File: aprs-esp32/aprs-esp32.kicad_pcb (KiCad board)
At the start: 4 copper layers, 100 x 100 mm, 47 parts, among them J1 GPS_CONNECTOR, J2 EXT_1WIRE, J3 PSU_CONN, J4 I2C, J5 M20-6102045, J6 RF_HI_LOW, J7 RF_OUT, J8 ESP PROGRAM, Q1 BSS138, Q2 BSS138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

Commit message: limpieza de esquematico
movi los level shifters a su propia pagina
movi la mayor parte de los conectores a una pagina separada
corregido: simbolos de pin desconectado faltantes
cambio: ESP renombrado a u2
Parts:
- renumbered ESP32-WROOM-32D1 to u2
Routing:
- added copper zone on B.Cu, net GND
- added copper zone on F.Cu, net GND
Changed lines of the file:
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@@
     (property "Sheetname" "")
     (attr smd)
-    (fp_text reference "ESP32-WROOM-32D1" (at -0.534725 12.101072 180) (layer "F.SilkS")
+    (fp_text reference "u2" (at -0.534725 12.101072 180) (layer "F.SilkS")
       (effects (font (size 1 1) (thickness 0.15)))
     )
@@
   (segment (start 63.785 97.1375) (end 63.2375 97.685) (width 0.2921) (layer "F.Cu") (net 54))
   (segment (start 63.785 94.215) (end 63.785 97.1375) (width 0.2921) (layer "F.Cu") (net 54))
-  (zone (net 18) (net_name "GND") (layer "In1.Cu") (name "GND") (hatch edge 0.508)
+  (zone (net 18) (net_name "GND") (layers "F.Cu" "In1.Cu" "B.Cu") (name "GND") (hatch edge 0.508)
     (priority 1)
     (connect_pads yes (clearance 0.8))

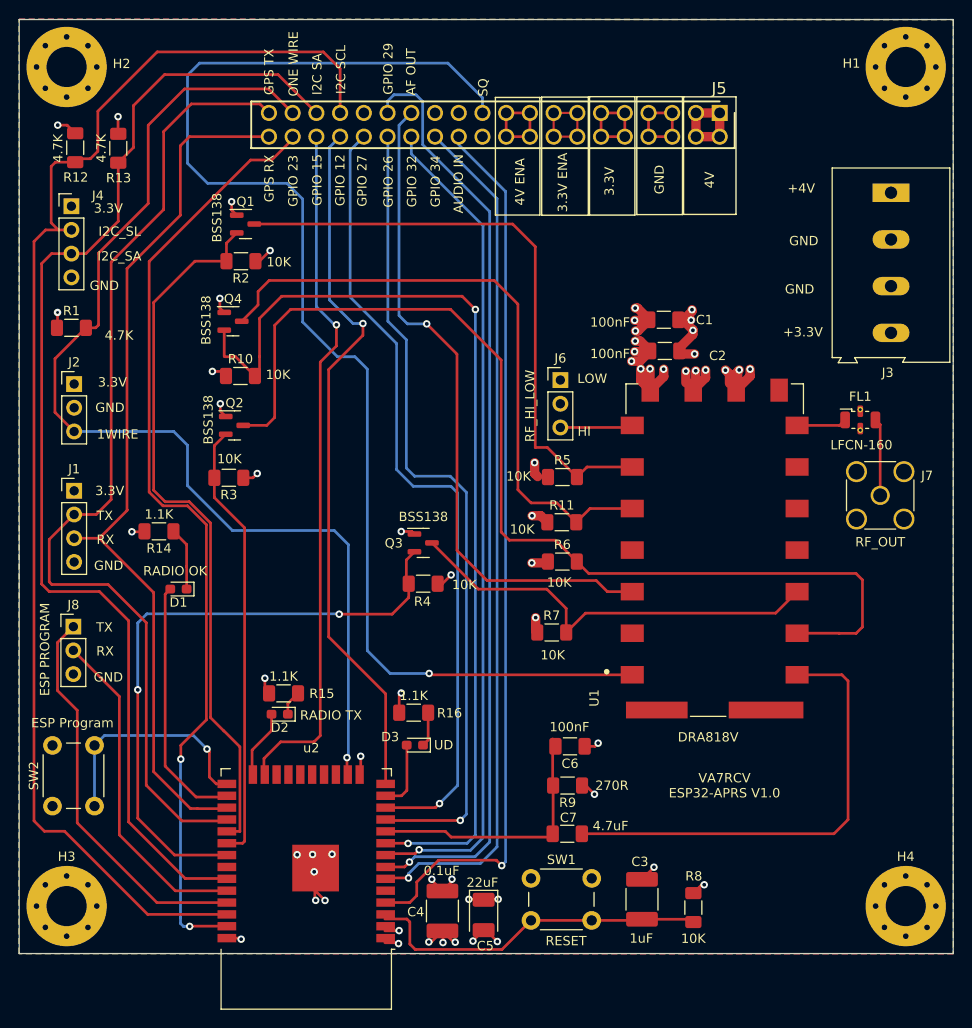
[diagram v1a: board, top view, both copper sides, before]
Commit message: multiple cambios en el ruteo
Todas las reglas de DRC pasan. solo hay warnings debido al silk screen
correcciones PCB:
- VDD para ESP y DRA ruteado via capacitores
- multiple conecciones a VDD cambiadas para evitar tombstoning

Optimizaciones PCB:
- algunos tracks fueron ruteados para reducir largo.
- todas las etiquetas fueron alienadas y/o movidas para hacer mas claro a quce componente corresponden.

cambios al proyecto:
- corregido tama;o de vias para +4v
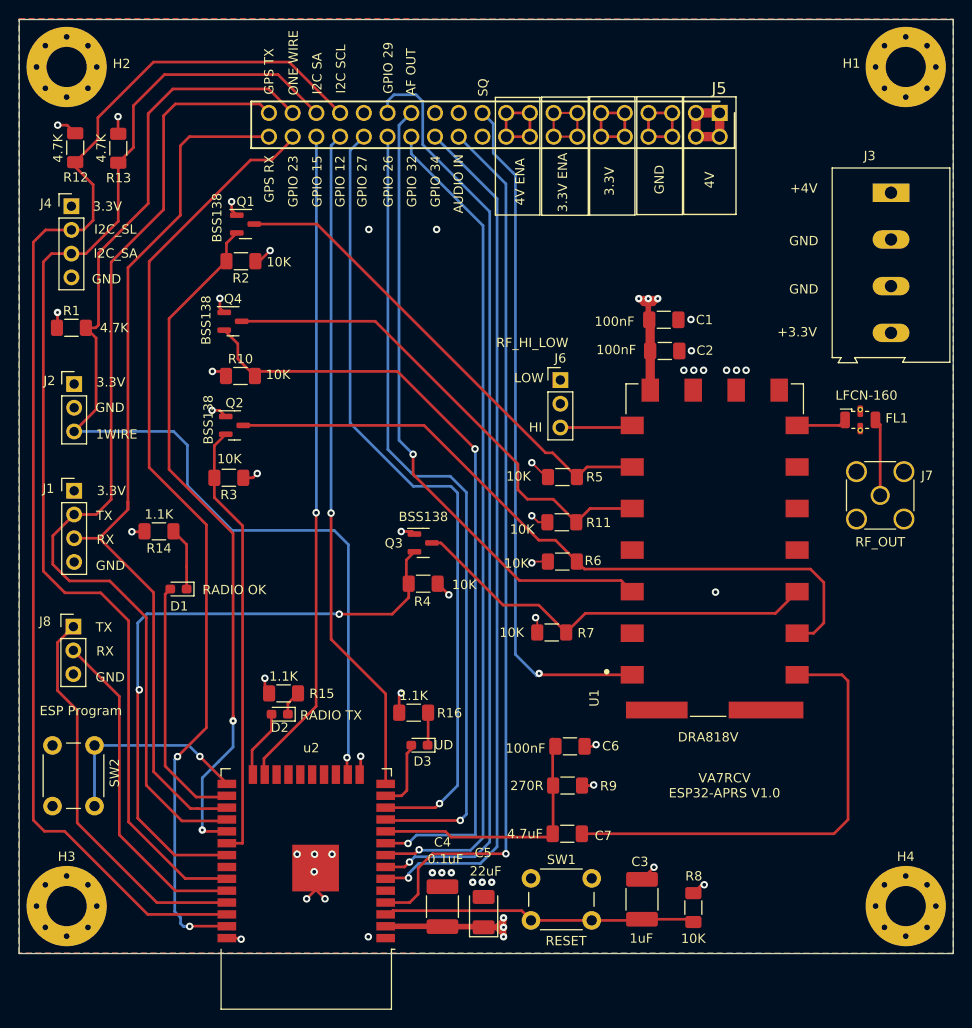
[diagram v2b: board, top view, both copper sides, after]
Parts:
- moved D3 0.49 mm to (62.9, 97.7)
- moved C4 0.46 mm to (65.3, 115.0), turned to 90 degrees
- moved C5 0.30 mm to (69.7, 115.6), turned to 90 degrees
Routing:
- net SQ: track 140.4 -> 73.1 mm
- net RADIO_TX_HIGH: track 112.3 -> 76.8 mm
- net GND: track 74.4 -> 39.4 mm, vias 30 -> 32
- net PTT_LOW: track 104.3 -> 84.8 mm
- net PTT_HIGH: track 67.4 -> 53.0 mm
- net RADIO_ENA_HIGH: track 64.7 -> 52.1 mm
- net +3V3: track 39.3 -> 48.4 mm, vias 17 -> 15
- net I2C_SCL: track 142.5 -> 137.7 mm
- net +4V: track 36.7 -> 32.1 mm, vias 13 -> 7
- net GPIO015: track 75.1 -> 71.1 mm
- net ESP_ENA: track 37.2 -> 33.4 mm
- net GPIO012: track 75.9 -> 72.1 mm
- net AF_OUT: track 71.8 -> 68.5 mm
- net ESP_PROG: track 24.9 -> 22.4 mm
- net RADIO_ENA_LOW: track 76.1 -> 74.4 mm, vias 0 -> 2
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
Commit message: pcb actualizado
- leds de status estan ahora juntos y visibles
- level shifters estan ahora juntos al centro
- capacitores de bypass estan ruteados correctamente.
- capacitores de bypass estan ordenados correctamente (valor ascendnte desde el circuito)
- lineas i2c estan ruteadas mas lejos del borde del pcb.
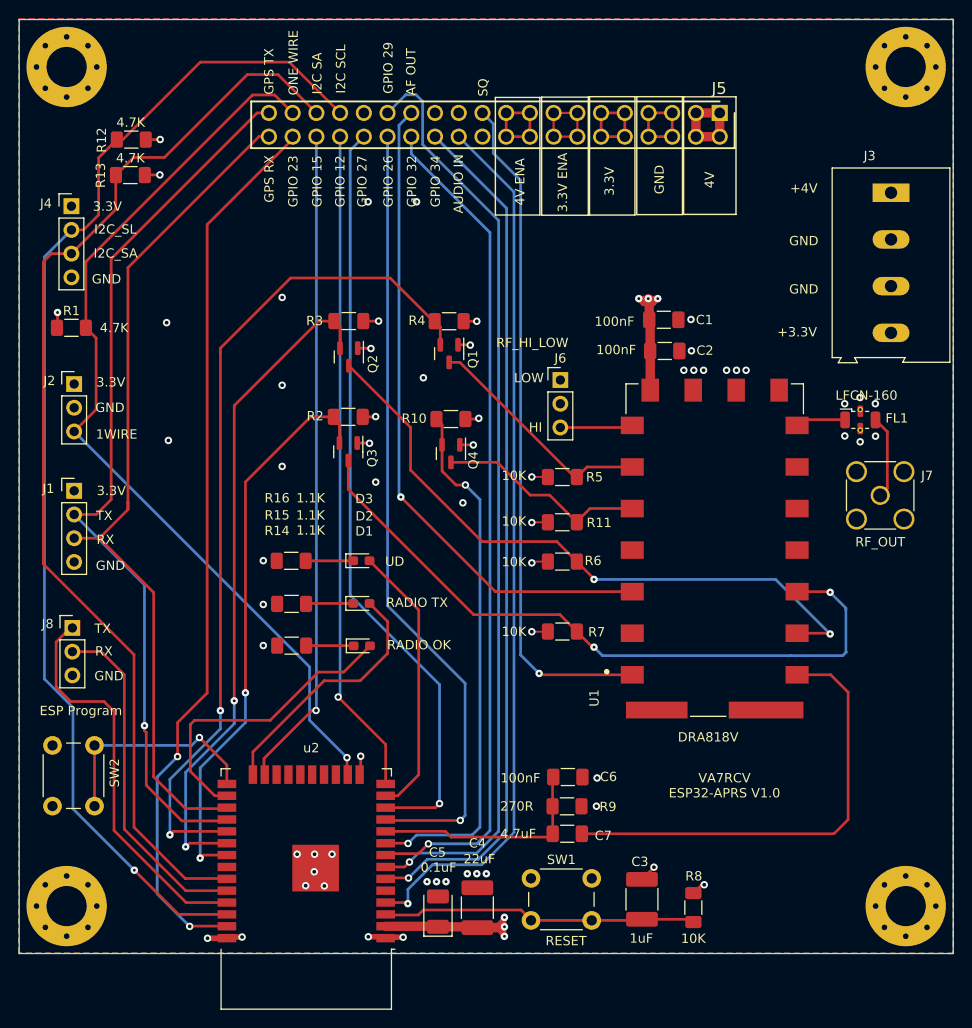
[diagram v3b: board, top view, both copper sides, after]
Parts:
- moved Q4 27.3 mm to (66.2, 66.5), turned to -90 degrees
- moved Q1 25.8 mm to (66.0, 55.8), turned to -90 degrees
- moved R4 23.2 mm to (66.0, 52.3)
- moved R10 23.0 mm to (66.2, 62.8), turned to 180 degrees
- moved R3 21.1 mm to (55.3, 52.3)
- moved R16 20.9 mm to (49.1, 78.0)
- moved D3 20.7 mm to (56.6, 77.9), turned to 0 degrees
- moved D1 20.6 mm to (56.7, 87.1), turned to 0 degrees
- moved R2 19.6 mm to (55.2, 62.5)
- moved R14 18.8 mm to (49.2, 87.0)
- moved D2 14.7 mm to (56.6, 82.5), turned to 0 degrees
- moved Q2 14.3 mm to (55.3, 56.1), turned to -90 degrees
- moved Q3 12.6 mm to (55.2, 66.3), turned to -90 degrees
- moved R15 9.62 mm to (49.2, 82.6)
- moved R12 6.07 mm to (32.0, 32.9), turned to 180 degrees
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- renumbered R4 to R2, R2 to R4
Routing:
- net PTT_HIGH: track 53.0 -> 22.7 mm
- net RADIO_RX_HIGH: track 44.9 -> 74.6 mm, vias 0 -> 2
- net PTT_LOW: track 84.8 -> 57.0 mm
- net RADIO_ENA_HIGH: track 52.1 -> 25.1 mm
- net RADIO_TX_LOW: track 46.9 -> 71.6 mm, vias 0 -> 2
- net GPIO014: track 7.55 -> 29.6 mm
- net GPIO02: track 7.82 -> 27.4 mm
- net ONE_WIRE: track 118.5 -> 99.3 mm
- net RADIO_ENA_LOW: track 74.4 -> 91.4 mm
- net GPS_TX: track 106.7 -> 95.7 mm, vias 0 -> 1
- net I2C_SCL: track 137.7 -> 127.6 mm, vias 0 -> 1
- net RADIO_TX_HIGH: track 76.8 -> 69.7 mm, vias 0 -> 2
- net RADIO_RX_LOW: track 67.1 -> 60.7 mm
- net I2C_SA: track 124.0 -> 117.5 mm
- net GPIO04: track 26.7 -> 32.7 mm
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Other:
- board text removed: "BSS138"

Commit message: cambios a la lineas de poder
-Modifique la isla de 4v para que sea mas peque;a
-Cambie el ruteo de varios tracks para hacerlos mas cortos
-modificado la ubicacion de algunas vias para que las lineas de tierra esten mas cercanas a los pads
-capacitores de bypass de ESP estan 1mm mas cerca.
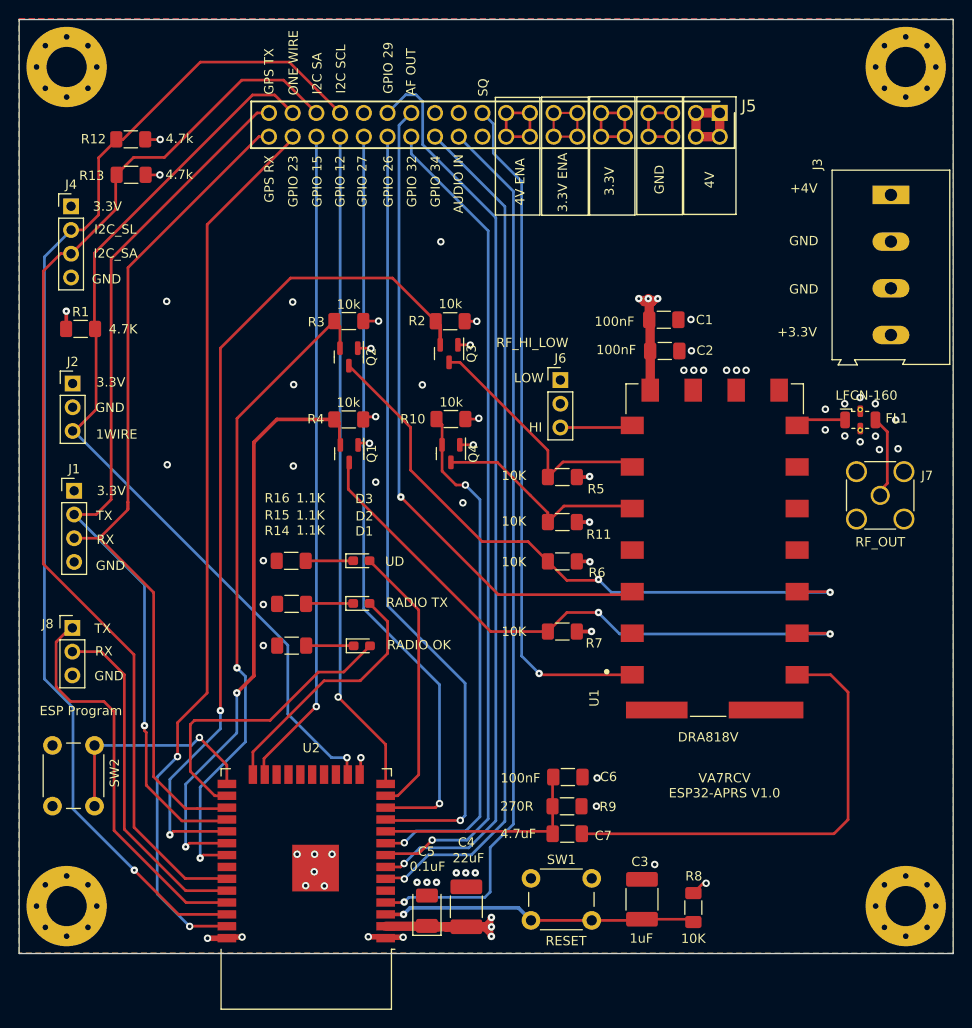
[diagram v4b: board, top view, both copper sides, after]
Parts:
- moved Q1 15.1 mm to (55.3, 66.5)
- moved Q3 15.1 mm to (66.0, 55.8)
- moved R4 15.0 mm to (55.3, 62.8)
- moved R2 15.0 mm to (66.1, 52.3)
- moved C4 1.18 mm to (67.9, 115.0)
- moved C5 1.18 mm to (63.7, 115.4)
- moved R1 0.99 mm to (26.6, 53.1)
- moved J3 0.23 mm to (113.3, 38.8)
- moved J2 0.17 mm to (25.7, 59.0)
- moved R13 0.09 mm to (32.0, 36.6)
- moved R12 0.07 mm to (31.9, 32.8)
- turned R11 to 180 degrees
- turned R6 to 180 degrees
- turned R5 to 180 degrees
- turned R7 to 180 degrees
- renumbered u2 to U2
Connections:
- Q1 pad 2: RADIO_ENA_LOW -> RADIO_TX_LOW
- Q1 pad 3: RADIO_ENA_HIGH -> RADIO_TX_HIGH
- Q2 pad 2: RADIO_TX_LOW -> RADIO_RX_LOW
- Q2 pad 3: RADIO_TX_HIGH -> RADIO_RX_HIGH
- Q3 pad 2: RADIO_RX_LOW -> RADIO_ENA_LOW
- Q3 pad 3: RADIO_RX_HIGH -> RADIO_ENA_HIGH
- R2 pad 2: RADIO_RX_LOW -> RADIO_ENA_LOW
- R3 pad 2: RADIO_TX_LOW -> RADIO_RX_LOW
- R4 pad 2: RADIO_ENA_LOW -> RADIO_TX_LOW
- R6 pad 2: RADIO_TX_HIGH -> RADIO_RX_HIGH
- R7 pad 2: RADIO_RX_HIGH -> RADIO_TX_HIGH
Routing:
- net RADIO_RX_LOW: track 60.7 -> 70.4 mm
- net RADIO_TX_LOW: track 71.6 -> 63.6 mm
- net RADIO_RX_HIGH: track 74.6 -> 67.8 mm
- net RADIO_TX_HIGH: track 69.7 -> 66.3 mm
- net +3V3: track 44.4 -> 47.0 mm
- net RADIO_ENA_HIGH: track 25.1 -> 27.3 mm
- net GND: track 34.7 -> 32.7 mm, vias 47 -> 51
- net AUDIO_IN: track 94.8 -> 96.0 mm
- net GPIO27: track 81.9 -> 80.8 mm
- net GPIO35: track 99.6 -> 98.6 mm
- net I2C_SA: track 117.5 -> 116.5 mm
- net GPIO032: track 89.4 -> 88.4 mm
- net GPIO34: track 92.1 -> 91.3 mm
- net +4V: track 31.4 -> 30.6 mm
- net PTT_HIGH: track 22.7 -> 23.5 mm
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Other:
- board text added: "10k"
- board text added: "4.7k"

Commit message: ADDED: ground vias en donde la sen~al cambia de plano
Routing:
- net GND: vias 51 -> 67
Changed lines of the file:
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@@
     (property "Sheetname" "")
     (attr smd)
-    (fp_text reference "C4" (at 6.8955 0.01) (layer "F.SilkS")
-      (effects (font (size 1 1) (thickness 0.15)))
-    )
-    (fp_text value "0.1uF" (at 4.3025 -4.16) (layer "F.SilkS")
+    (fp_text reference "C4" (at 2.2475 3.24) (layer "F.SilkS")
+      (effects (font (size 1 1) (thickness 0.15)))
+    )
+    (fp_text value "0.1uF" (at -3.8425 0.1) (layer "F.SilkS")
       (effects (font (size 1 1) (thickness 0.15)))
     )
@@
     (property "Sheetname" "")
     (attr smd)
-    (fp_text reference "C5" (at 6.341 -0.05) (layer "F.SilkS")
-      (effects (font (size 1 1) (thickness 0.15)))
-    )
-    (fp_text value "22uF" (at 5.635 4.44) (layer "F.SilkS")
+    (fp_text reference "C5" (at 4.07 -0.03) (layer "F.SilkS")
+      (effects (font (size 1 1) (thickness 0.15)))
+    )
+    (fp_text value "22uF" (at -3.45 -0.06) (layer "F.SilkS")
       (effects (font (size 1 1) (thickness 0.15)))
     )
@@
   (segment (start 45.47 30) (end 46.74 30) (width 0.2921) (layer "F.Cu") (net 14))
   (segment (start 29.8474 45.6226) (end 45.47 30) (width 0.2921) (layer "F.Cu") (net 14))
-  (segment (start 33.415 95.605) (end 33.415 96.135) (width 0.2921) (layer "F.Cu") (net 14))
+  (segment (start 25.885 72.995) (end 28.2472 72.995) (width 0.2921) (layer "F.Cu") (net 14))
+  (segment (start 33.415 95.605) (end 33.415 101.795) (width 0.2921) (layer "F.Cu") (net 14))
   (segment (start 37.425 105.805) (end 41.814203 105.805) (width 0.2921) (layer "F.Cu") (net 14))
-  (segment (start 25.885 72.995) (end 28.2472 72.995) (width 0.2921) (layer "F.Cu") (net 14))
-  (segment (start 33.415 96.135) (end 33.605 96.325) (width 0.2921) (layer "F.Cu") (net 14))
   (segment (start 29.8474 71.3948) (end 29.8474 45.6226) (width 0.2921) (layer "F.Cu") (net 14))
   (segment (start 28.2472 72.995) (end 29.8474 71.3948) (width 0.2921) (layer "F.Cu") (net 14))
-  (segment (start 33.605 96.325) (end 33.605 101.985) (width 0.2921) (layer "F.Cu") (net 14))
-  (segment (start 33.605 101.985) (end 37.425 105.805) (width 0.2921) (layer "F.Cu") (net 14))
+  (segment (start 33.415 101.795) (end 37.425 105.805) (width 0.2921) (layer "F.Cu") (net 14))
   (via (at 33.415 95.605) (size 0.8) (drill 0.3) (layers "F.Cu" "B.Cu") (net 14))
   (segment (start 33.415 80.525) (end 33.415 95.605) (width 0.2921) (layer "B.Cu") (net 14))
@@
   (segment (start 89.92 30) (end 89.92 32.54) (width 0.2921) (layer "F.Cu") (net 18))
   (via (at 46.14281 82.625) (size 0.8) (drill 0.4) (layers "F.Cu" "B.Cu") (net 18))
+  (via (at 37.395 117.705) (size 0.8) (drill 0.3) (layers "F.Cu" "B.Cu") (free) (net 18))
   (via (at 50.675 112.735) (size 0.8) (drill 0.4) (layers "F.Cu" "B.Cu") (net 18))
   (via (at 111.685 64.605) (size 0.8) (drill 0.4) (layers "F.Cu" "B.Cu") (free) (net 18))
@@
   (via (at 63.655 112.37) (size 0.8) (drill 0.3) (layers "F.Cu" "B.Cu") (net 18))
   (via (at 93.275 57.55) (size 0.8) (drill 0.4) (layers "F.Cu" "B.Cu") (free) (net 18))
+  (via (at 107.975 85.785) (size 0.8) (drill 0.3) (layers "F.Cu" "B.Cu") (free) (net 18))
+  (via (at 54.815 97.895) (size 0.8) (drill 0.3) (layers "F.Cu" "B.Cu") (free) (net 18))
   (via (at 66.799 111.36) (size 0.8) (drill 0.3) (layers "F.Cu" "B.Cu") (net 18))
   (via (at 110.04 65.215) (size 0.8) (drill 0.4) (layers "F.Cu" "B.Cu") (free) (net 18))
+  (via (at 61.815 70.535) (size 0.8) (drill 0.3) (layers "F.Cu" "B.Cu") (free) (net 18))
   (via (at 53.4948 109.3678) (size 0.8) (drill 0.4) (layers "F.Cu" "B.Cu") (net 18))
+  (via (at 31.725 111.875) (size 0.8) (drill 0.3) (layers "F.Cu" "B.Cu") (free) (net 18))
   (via (at 67.815 111.36) (size 0.8) (drill 0.3) (layers "F.Cu" "B.Cu") (net 18))
   (via (at 91.925 52.1162) (size 0.8) (drill 0.4) (layers "F.Cu" "B.Cu") (free) (net 18))
+  (via (at 81.405 80.805) (size 0.8) (drill 0.3) (layers "F.Cu" "B.Cu") (free) (net 18))
   (via (at 40.165 118.365) (size 0.8) (drill 0.4) (layers "F.Cu" "B.Cu") (net 18))
   (via (at 96.8018 57.55) (size 0.8) (drill 0.4) (layers "F.Cu" "B.Cu") (free) (net 18))
   (via (at 106.305 63.935) (size 0.8) (drill 0.4) (layers "F.Cu" "B.Cu") (free) (net 18))
+  (via (at 66.735 104.735) (size 0.8) (drill 0.3) (layers "F.Cu" "B.Cu") (free) (net 18))
   (via (at 61.105 118.255) (size 0.8) (drill 0.4) (layers "F.Cu" "B.Cu") (net 18))
+  (via (at 35.825 108.335) (size 0.8) (drill 0.3) (layers "F.Cu" "B.Cu") (free) (net 18))
   (via (at 51.5898 111.2474) (size 0.8) (drill 0.4) (layers "F.Cu" "B.Cu") (net 18))
   (via (at 64.685 112.37) (size 0.8) (drill 0.3) (layers "F.Cu" "B.Cu") (net 18))
@@
   (via (at 49.761 109.3678) (size 0.8) (drill 0.4) (layers "F.Cu" "B.Cu") (net 18))
   (via (at 46.14281 77.935) (size 0.8) (drill 0.4) (layers "F.Cu" "B.Cu") (free) (net 18))
+  (via (at 37.435 109.665) (size 0.8) (drill 0.3) (layers "F.Cu" "B.Cu") (free) (net 18))
   (via (at 35.795 50.175) (size 0.8) (drill 0.4) (layers "F.Cu" "B.Cu") (free) (net 18))
   (via (at 49.385 59.085) (size 0.8) (drill 0.4) (layers "F.Cu" "B.Cu") (free) (net 18))
+  (via (at 64.015 103.315) (size 0.8) (drill 0.3) (layers "F.Cu" "B.Cu") (free) (net 18))
   (via (at 106.315 61.725) (size 0.8) (drill 0.4) (layers "F.Cu" "B.Cu") (free) (net 18))
   (via (at 35.855 67.665) (size 0.8) (drill 0.4) (layers "F.Cu" "B.Cu") (free) (net 18))
@@
   (via (at 46.14281 87.025) (size 0.8) (drill 0.4) (layers "F.Cu" "B.Cu") (net 18))
   (via (at 108.385 61.135) (size 0.8) (drill 0.4) (layers "F.Cu" "B.Cu") (free) (net 18))
+  (via (at 52.205 94.535) (size 0.8) (drill 0.3) (layers "F.Cu" "B.Cu") (free) (net 18))
   (via (at 95.735 57.55) (size 0.8) (drill 0.4) (layers "F.Cu" "B.Cu") (free) (net 18))
   (via (at 68.835 111.36) (size 0.8) (drill 0.3) (layers "F.Cu" "B.Cu") (net 18))
@@
   (via (at 113.845 62.875) (size 0.8) (drill 0.4) (layers "F.Cu" "B.Cu") (free) (net 18))
   (via (at 67.505 71.745) (size 0.8) (drill 0.4) (layers "F.Cu" "B.Cu") (free) (net 18))
+  (via (at 39.165 110.755) (size 0.8) (drill 0.3) (layers "F.Cu" "B.Cu") (free) (net 18))
   (via (at 62.595 112.375) (size 0.8) (drill 0.3) (layers "F.Cu" "B.Cu") (net 18))
   (via (at 49.285 50.245) (size 0.8) (drill 0.4) (layers "F.Cu" "B.Cu") (free) (net 18))
   (via (at 81.875 101.205) (size 0.8) (drill 0.4) (layers "F.Cu" "B.Cu") (net 18))
+  (via (at 75.715 91.135) (size 0.8) (drill 0.3) (layers "F.Cu" "B.Cu") (free) (net 18))
+  (via (at 107.935 81.325) (size 0.8) (drill 0.3) (layers "F.Cu" "B.Cu") (free) (net 18))
+  (via (at 54.085 93.755) (size 0.8) (drill 0.3) (layers "F.Cu" "B.Cu") (free) (net 18))
   (via (at 81.805 104.225) (size 0.8) (drill 0.4) (layers "F.Cu" "B.Cu") (net 18))
+  (via (at 81.285 82.665) (size 0.8) (drill 0.3) (layers "F.Cu" "B.Cu") (free) (net 18))
   (via (at 112.105 66.045) (size 0.8) (drill 0.4) (layers "F.Cu" "B.Cu") (free) (net 18))
   (segment (start 37.83 113.27) (end 42.235 113.27) (width 0.2921) (layer "F.Cu") (net 19))
